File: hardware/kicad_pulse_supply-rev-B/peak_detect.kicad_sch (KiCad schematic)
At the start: 62 parts, among them J2 OPT_PWR, U3 LTC6244CMS8

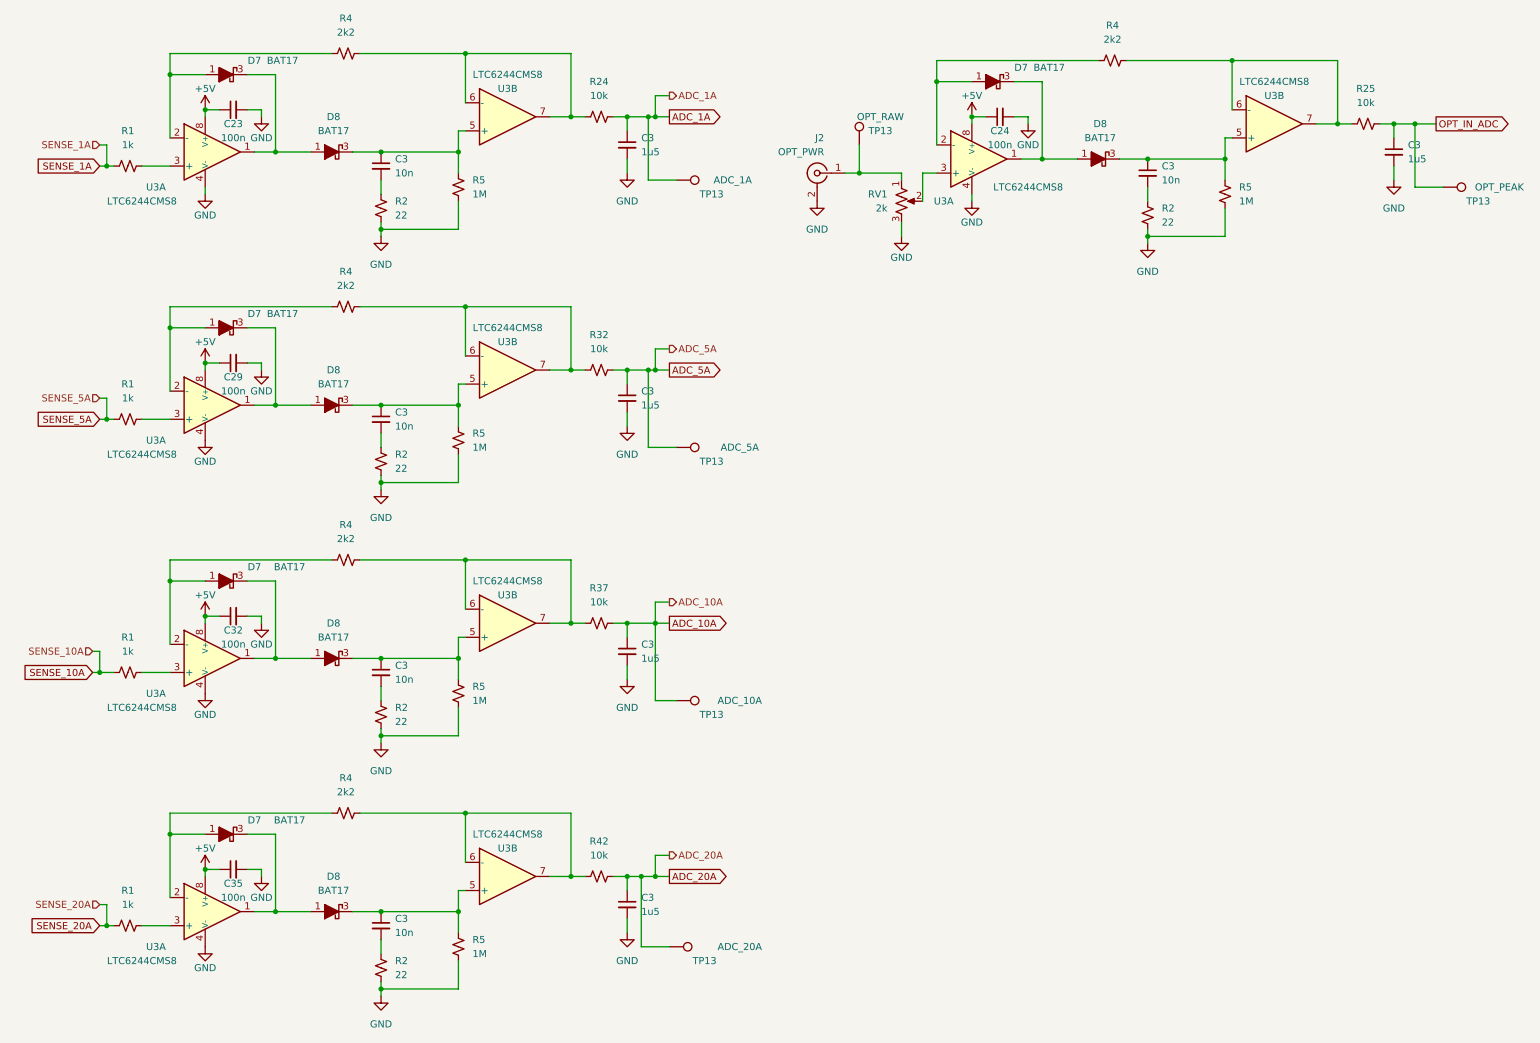
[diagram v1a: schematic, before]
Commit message: Working on TPS55289 boost issues
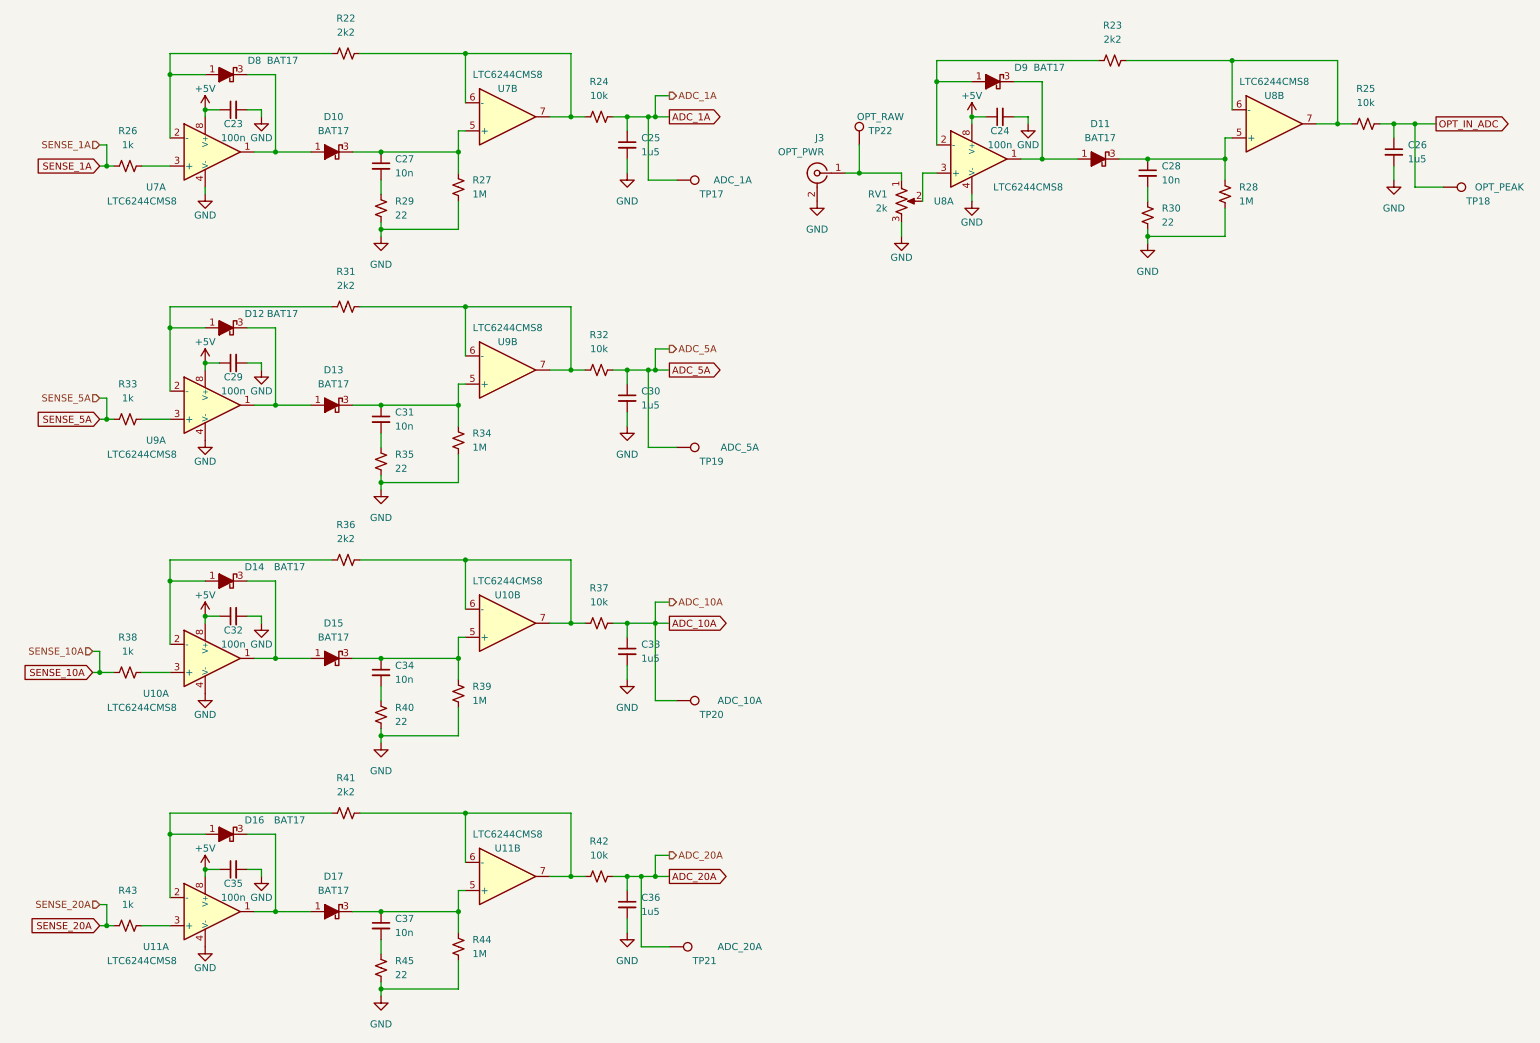
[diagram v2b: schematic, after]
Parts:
- renumbered C3 to C25, C3 to C26, C3 to C27, C3 to C28, C3 to C30, C3 to C31, C3 to C33, C3 to C34, C3 to C36, C3 to C37, D8 to D10, D8 to D11, D7 to D12, D8 to D13, D7 to D14, D8 to D15, D7 to D16, D8 to D17, D7 to D8, D7 to D9, J2 to J3, R4 to R22, R4 to R23, R1 to R26, R5 to R27, R5 to R28, R2 to R29, R2 to R30, R4 to R31, R1 to R33, R5 to R34, R2 to R35, R4 to R36, R1 to R38, R5 to R39, R2 to R40, R4 to R41, R1 to R43, R5 to R44, R2 to R45, TP13 to TP17, TP13 to TP18, TP13 to TP19, TP13 to TP20, TP13 to TP21, TP13 to TP22, U3 to U10, U3 to U11, U3 to U7, U3 to U8, U3 to U9
